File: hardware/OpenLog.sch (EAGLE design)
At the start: 20 parts, among them Q1 16MHZ, U1 ATMEGA328P_TQFP, U2 3.3V MIC5205, U3 microSD Socket

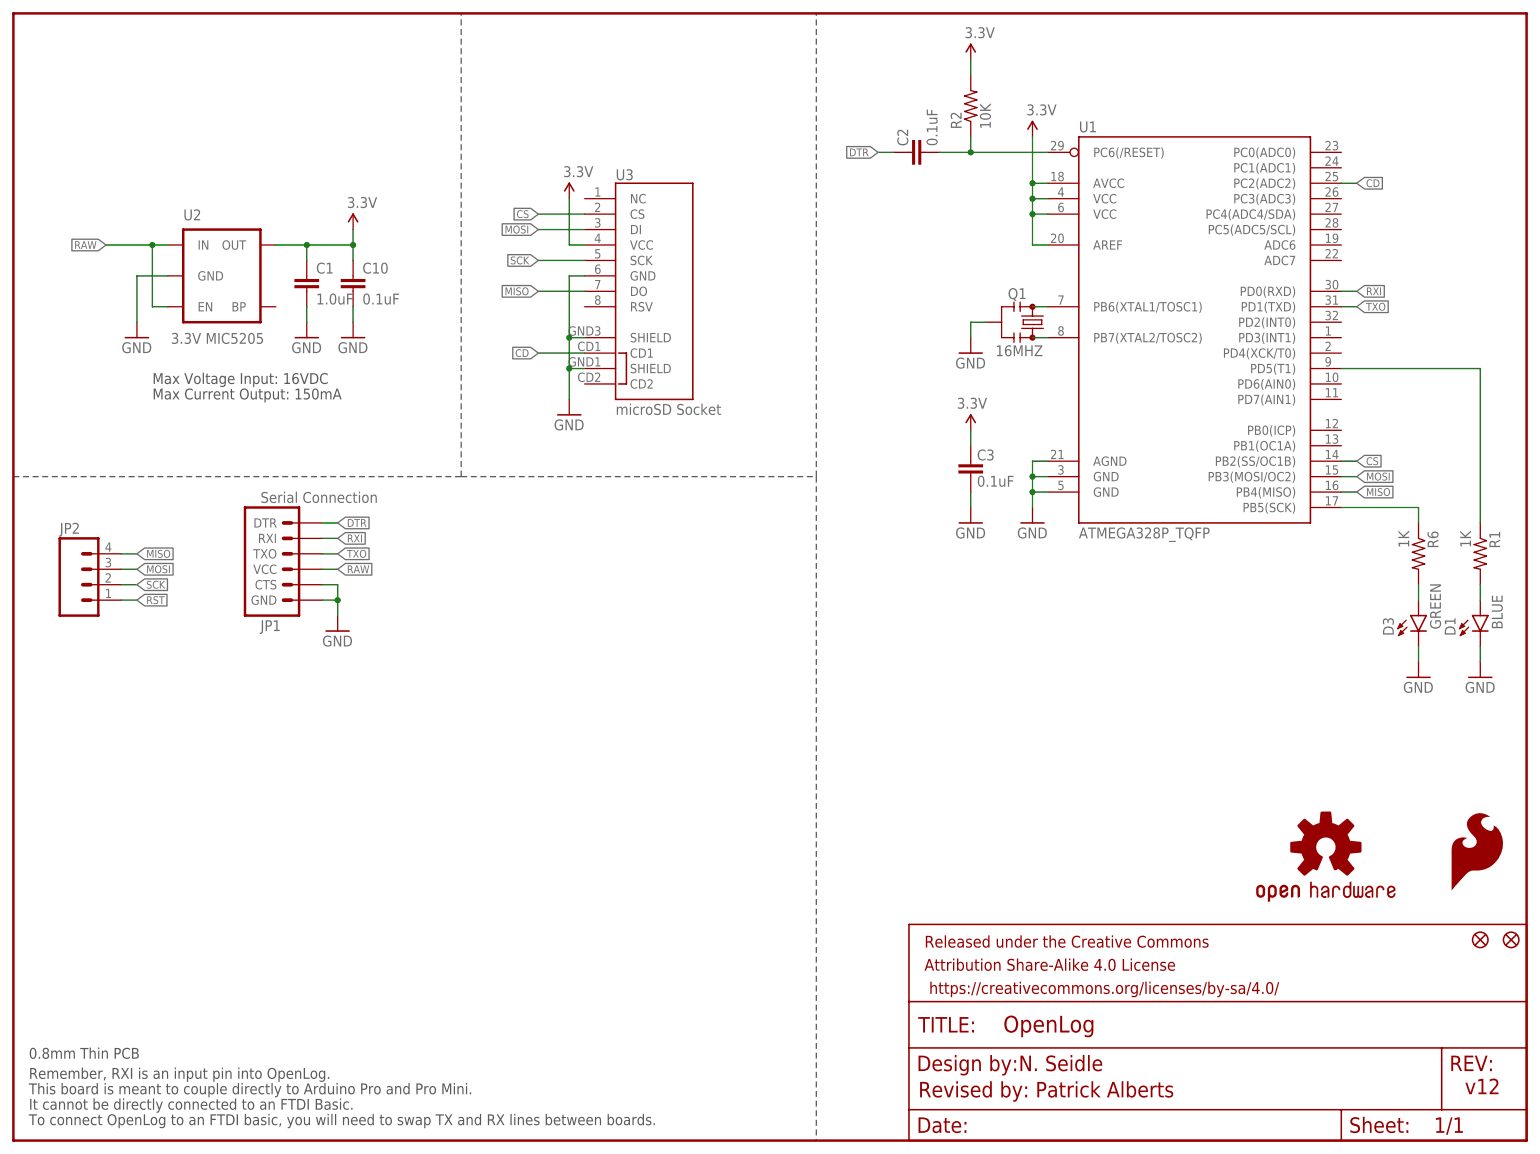
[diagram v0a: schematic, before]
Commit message: Added Test point , removed OSHW logo
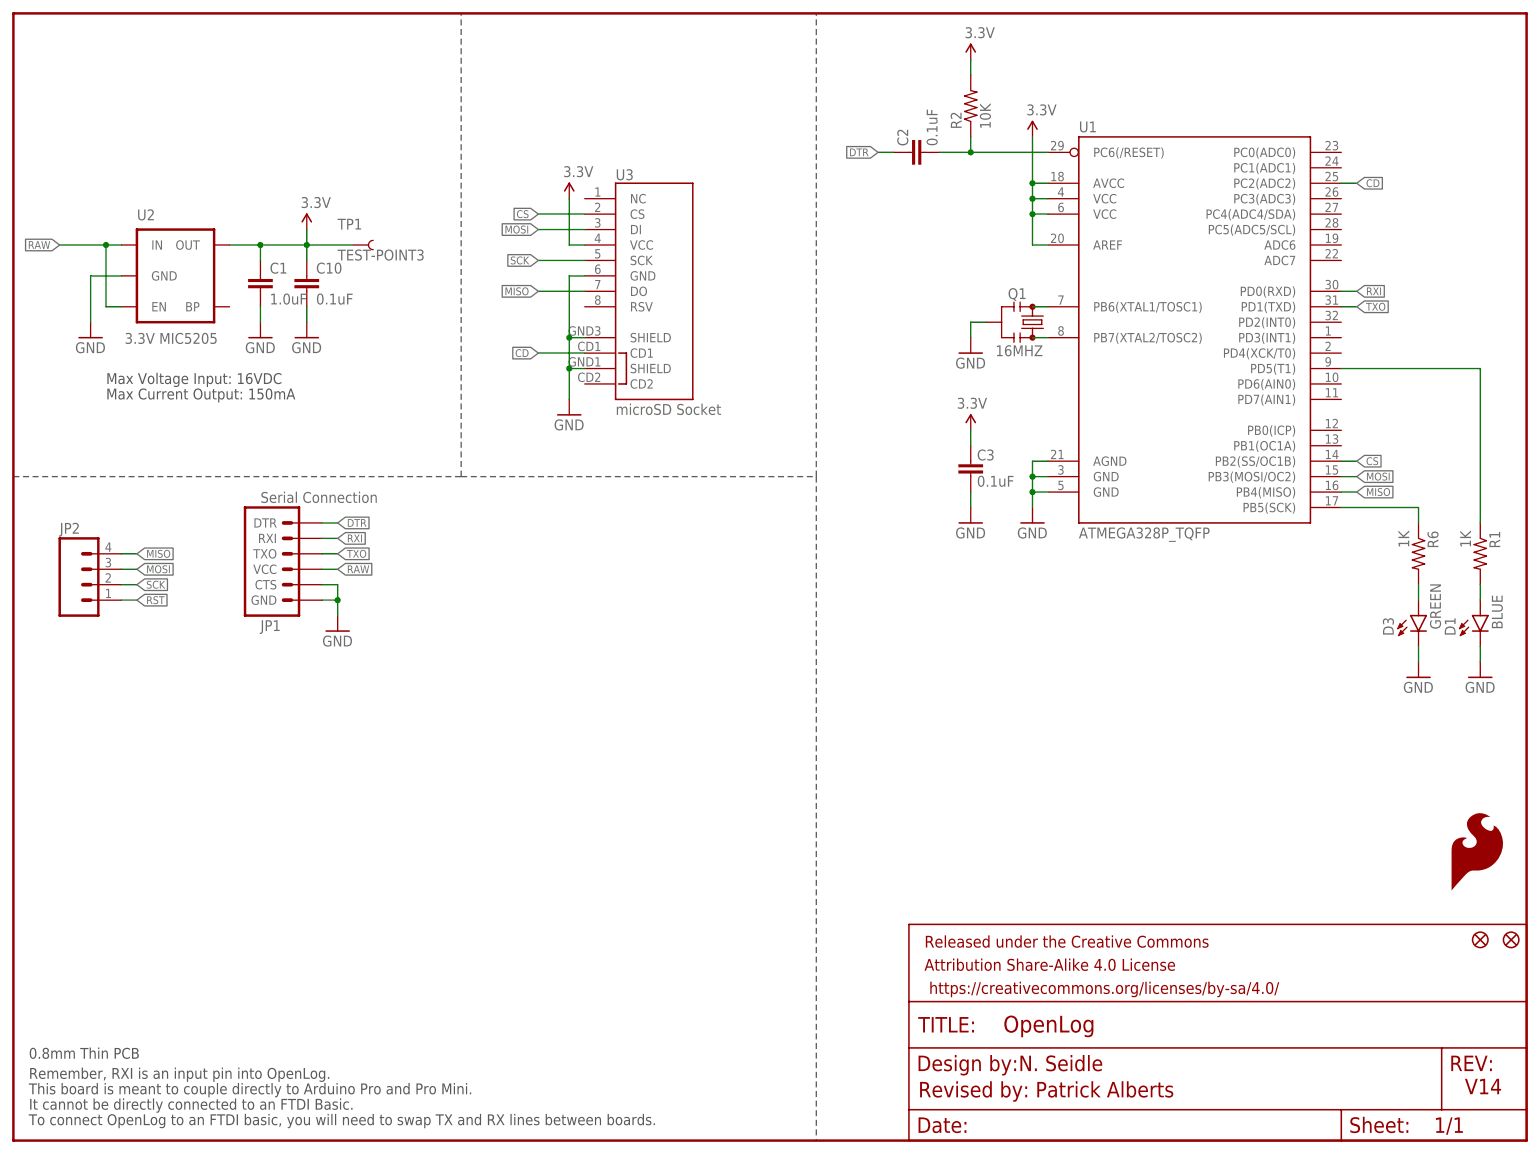
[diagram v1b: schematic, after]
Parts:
- removed LOGO2: OSHW-LOGOS, SparkFun-Aesthetics:OSHW-LOGOS
- added TP1: TEST-POINT3, SparkFun-Passives:TEST-POINT3
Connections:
- net 3.3V: now also TP1.1
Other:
- note added: "V14"
- note removed: "v12"
- moved on the sheet: C1, C10, U2
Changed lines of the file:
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@@
 <part name="FID2" library="SparkFun-Aesthetics" deviceset="FIDUCIAL" device="UFIDUCIAL"/>
 <part name="GND6" library="SparkFun" deviceset="GND" device=""/>
-<part name="LOGO2" library="SparkFun-Aesthetics" deviceset="OSHW-LOGO" device="S"/>
+<part name="TP1" library="SparkFun-Passives" deviceset="TEST-POINT" device="3"/>
 </parts>
 <sheets>
 <sheet>
 <plain>
-<text x="22.86" y="124.46" size="1.778" layer="97">Max Voltage Input: 16VDC</text>
-<text x="22.86" y="121.92" size="1.778" layer="97">Max Current Output: 150mA</text>
+<text x="15.24" y="124.46" size="1.778" layer="97">Max Voltage Input: 16VDC</text>
+<text x="15.24" y="121.92" size="1.778" layer="97">Max Current Output: 150mA</text>
 <text x="2.54" y="10.16" size="1.778" layer="97">Remember, RXI is an input pin into OpenLog.</text>
 <text x="2.54" y="7.62" size="1.778" layer="97">This board is meant to couple directly to Arduino Pro and Pro Mini.</text>
 <text x="2.54" y="5.08" size="1.778" layer="97">It cannot be directly connected to an FTDI Basic.</text>
 <text x="2.54" y="2.54" size="1.778" layer="97">To connect OpenLog to an FTDI basic, you will need to swap TX and RX lines between boards.</text>
-<text x="238.76" y="7.62" size="2.54" layer="94">v12</text>
+<text x="238.76" y="7.62" size="2.54" layer="94">V14</text>
 <text x="165.354" y="11.43" size="2.54" layer="94">N. Seidle</text>
 <text x="148.844" y="7.112" size="2.54" layer="94">Revised by: Patrick Alberts</text>
@@
 </plain>
 <instances>
-<instance part="C10" gate="G$1" x="55.88" y="139.7"/>
+<instance part="C10" gate="G$1" x="48.26" y="139.7"/>
 <instance part="FRAME1" gate="G$1" x="0" y="0"/>
 <instance part="FRAME1" gate="V" x="147.32" y="0"/>
-<instance part="GND25" gate="1" x="48.26" y="132.08"/>
-<instance part="GND26" gate="1" x="55.88" y="132.08"/>
+<instance part="GND25" gate="1" x="40.64" y="132.08"/>
+<instance part="GND26" gate="1" x="48.26" y="132.08"/>
 <instance part="R2" gate="G$1" x="157.48" y="170.18" rot="R90"/>
 <instance part="C3" gate="G$1" x="157.48" y="111.76" smashed="yes" rot="R180">
@@
 </instance>
 <instance part="GND8" gate="1" x="231.14" y="76.2"/>
-<instance part="U2" gate="G$1" x="35.56" y="142.24" smashed="yes">
-<attribute name="NAME" x="27.94" y="151.384" size="1.778" layer="95"/>
-<attribute name="VALUE" x="25.908" y="131.064" size="1.778" layer="96"/>
-</instance>
-<instance part="GND30" gate="1" x="20.32" y="132.08"/>
+<instance part="U2" gate="G$1" x="27.94" y="142.24" smashed="yes">
+<attribute name="NAME" x="20.32" y="151.384" size="1.778" layer="95"/>
+<attribute name="VALUE" x="18.288" y="131.064" size="1.778" layer="96"/>
+</instance>
+<instance part="GND30" gate="1" x="12.7" y="132.08"/>
 <instance part="P+11" gate="G$1" x="157.48" y="177.8"/>
-<instance part="P+12" gate="G$1" x="55.88" y="149.86"/>
+<instance part="P+12" gate="G$1" x="48.26" y="149.86"/>
 <instance part="P+15" gate="G$1" x="157.48" y="116.84" smashed="yes">
 <attribute name="VALUE" x="155.194" y="120.396" size="1.778" layer="96"/>
@@
 </instance>
 <instance part="GND2" gate="1" x="241.3" y="76.2"/>
-<instance part="C1" gate="G$1" x="48.26" y="139.7"/>
+<instance part="C1" gate="G$1" x="40.64" y="139.7"/>
 <instance part="JP2" gate="G$1" x="12.7" y="91.44"/>
 <instance part="P+2" gate="G$1" x="91.44" y="154.94"/>
@@
 <instance part="FID2" gate="G$1" x="241.3" y="33.02"/>
 <instance part="GND6" gate="1" x="53.34" y="83.82"/>
-<instance part="LOGO2" gate="G$1" x="215.9" y="48.26"/>
+<instance part="TP1" gate="G$1" x="55.88" y="147.32"/>
 </instances>
 <busses>
@@
 <net name="GND" class="1">
 <segment>
-<wire x1="48.26" y1="134.62" x2="48.26" y2="137.16" width="0.1524" layer="91"/>
+<wire x1="40.64" y1="134.62" x2="40.64" y2="137.16" width="0.1524" layer="91"/>
 <pinref part="GND25" gate="1" pin="GND"/>
 <pinref part="C1" gate="G$1" pin="2"/>
 </segment>
 <segment>
-<wire x1="55.88" y1="134.62" x2="55.88" y2="137.16" width="0.1524" layer="91"/>
+<wire x1="48.26" y1="134.62" x2="48.26" y2="137.16" width="0.1524" layer="91"/>
 <pinref part="C10" gate="G$1" pin="2"/>
 <pinref part="GND26" gate="1" pin="GND"/>
@@
 </segment>
 <segment>
-<wire x1="25.4" y1="142.24" x2="20.32" y2="142.24" width="0.1524" layer="91"/>
-<wire x1="20.32" y1="142.24" x2="20.32" y2="134.62" width="0.1524" layer="91"/>
+<wire x1="17.78" y1="142.24" x2="12.7" y2="142.24" width="0.1524" layer="91"/>
+<wire x1="12.7" y1="142.24" x2="12.7" y2="134.62" width="0.1524" layer="91"/>
 <pinref part="U2" gate="G$1" pin="GND"/>
 <pinref part="GND30" gate="1" pin="GND"/>
@@
 <net name="RAW" class="1">
 <segment>
-<wire x1="22.86" y1="147.32" x2="25.4" y2="147.32" width="0.1524" layer="91"/>
-<wire x1="25.4" y1="137.16" x2="22.86" y2="137.16" width="0.1524" layer="91"/>
-<wire x1="22.86" y1="137.16" x2="22.86" y2="147.32" width="0.1524" layer="91"/>
-<wire x1="15.24" y1="147.32" x2="22.86" y2="147.32" width="0.1524" layer="91"/>
-<junction x="22.86" y="147.32"/>
+<wire x1="15.24" y1="147.32" x2="17.78" y2="147.32" width="0.1524" layer="91"/>
+<wire x1="17.78" y1="137.16" x2="15.24" y2="137.16" width="0.1524" layer="91"/>
+<wire x1="15.24" y1="137.16" x2="15.24" y2="147.32" width="0.1524" layer="91"/>
+<wire x1="7.62" y1="147.32" x2="15.24" y2="147.32" width="0.1524" layer="91"/>
+<junction x="15.24" y="147.32"/>
 <pinref part="U2" gate="G$1" pin="IN"/>
 <pinref part="U2" gate="G$1" pin="EN"/>
-<label x="15.24" y="147.32" size="1.27" layer="95" rot="R180" xref="yes"/>
+<label x="7.62" y="147.32" size="1.27" layer="95" rot="R180" xref="yes"/>
 </segment>
 <segment>
@@
 <net name="3.3V" class="0">
 <segment>
-<wire x1="43.18" y1="147.32" x2="48.26" y2="147.32" width="0.1524" layer="91"/>
-<wire x1="48.26" y1="147.32" x2="55.88" y2="147.32" width="0.1524" layer="91"/>
-<wire x1="55.88" y1="147.32" x2="55.88" y2="149.86" width="0.1524" layer="91"/>
-<wire x1="55.88" y1="147.32" x2="55.88" y2="144.78" width="0.1524" layer="91"/>
+<wire x1="35.56" y1="147.32" x2="40.64" y2="147.32" width="0.1524" layer="91"/>
+<wire x1="40.64" y1="147.32" x2="48.26" y2="147.32" width="0.1524" layer="91"/>
+<wire x1="48.26" y1="147.32" x2="48.26" y2="149.86" width="0.1524" layer="91"/>
 <wire x1="48.26" y1="147.32" x2="48.26" y2="144.78" width="0.1524" layer="91"/>
-<junction x="55.88" y="147.32"/>
+<wire x1="40.64" y1="147.32" x2="40.64" y2="144.78" width="0.1524" layer="91"/>
 <junction x="48.26" y="147.32"/>
+<junction x="40.64" y="147.32"/>
 <pinref part="U2" gate="G$1" pin="OUT"/>
 <pinref part="P+12" gate="G$1" pin="3.3V"/>
 <pinref part="C10" gate="G$1" pin="1"/>
 <pinref part="C1" gate="G$1" pin="1"/>
-</segment>
-<segment>
+<pinref part="TP1" gate="G$1" pin="1"/>
+<wire x1="55.88" y1="147.32" x2="48.26" y2="147.32" width="0.1524" layer="91"/>
+</segment>
+<segment>

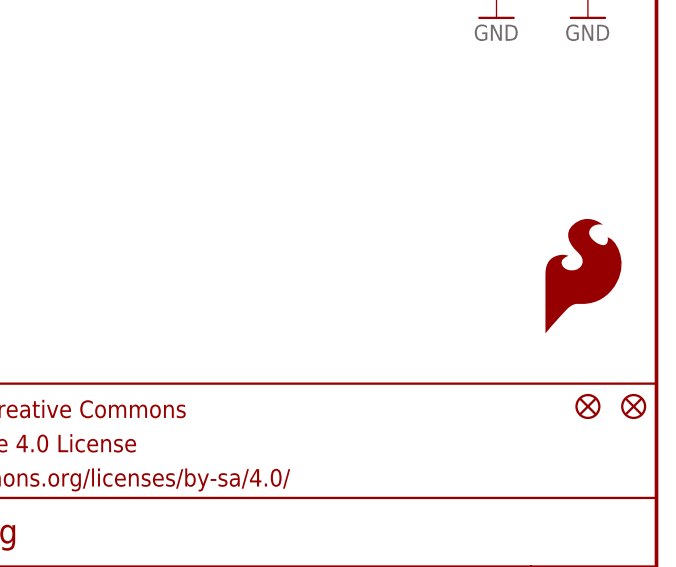
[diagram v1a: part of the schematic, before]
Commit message: Added OSHW logo, fixed trace
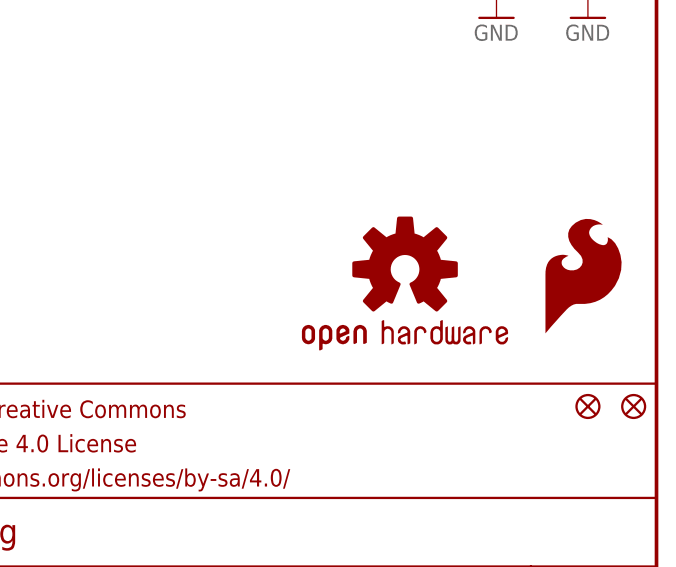
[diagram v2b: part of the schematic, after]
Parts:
- added LOGO2: OSHW-LOGOS, SparkFun-Aesthetics:OSHW-LOGOS
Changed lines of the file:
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@@
 <part name="GND6" library="SparkFun" deviceset="GND" device=""/>
 <part name="TP1" library="SparkFun-Passives" deviceset="TEST-POINT" device="3"/>
+<part name="LOGO2" library="SparkFun-Aesthetics" deviceset="OSHW-LOGO" device="S"/>
 </parts>
 <sheets>
@@
 <instance part="GND6" gate="1" x="53.34" y="83.82"/>
 <instance part="TP1" gate="G$1" x="55.88" y="147.32"/>
+<instance part="LOGO2" gate="G$1" x="220.98" y="48.26"/>
 </instances>
 <busses>
